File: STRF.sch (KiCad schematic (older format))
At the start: 38 parts, among them J1 USB_B_Micro, J2 SMA, J3 ARM 10pin, U1 XC6206P332MR, U2 USBLC6-2SC6, U3 STM32L432KBU6, U4 nRF24L01P, Y1 16MHz

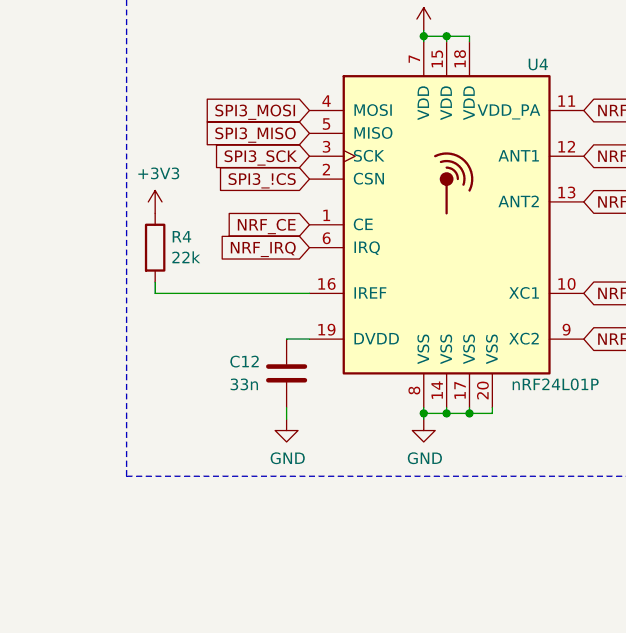
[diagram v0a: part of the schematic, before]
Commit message: Fixed IREF resistor to pull-down.
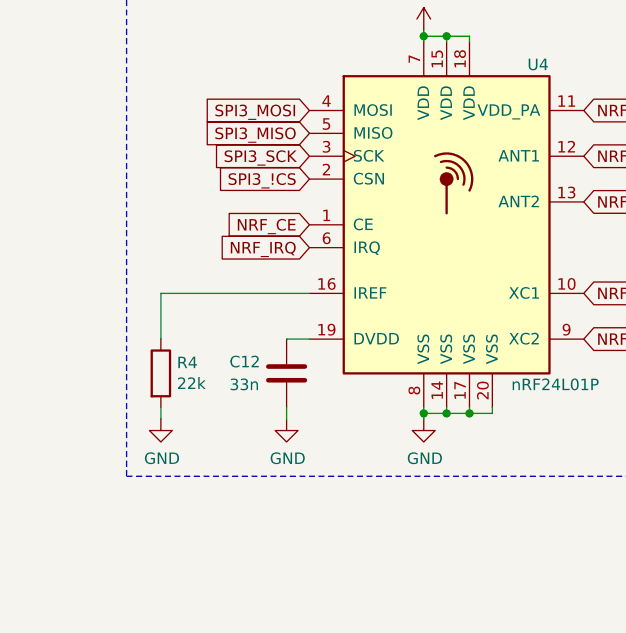
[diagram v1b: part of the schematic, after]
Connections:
- net +3V3: no longer R4.1
- net GND: now also R4.2
- net at U4.16 (IREF): now also R4.1; no longer R4.2
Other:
- moved on the sheet: R4
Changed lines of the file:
@@
 L Device:R R4
 U 1 1 5EC65DFA
-P 1075 5550
-F 0 "R4" H 1145 5596 50  0000 L CNN
-F 1 "22k" H 1145 5505 50  0000 L CNN
-F 2 "Resistor_SMD:R_0402_1005Metric" V 1005 5550 50  0001 C CNN
-F 3 "~" H 1075 5550 50  0001 C CNN
-	1    1075 5550
-	1    0    0    -1
-$EndComp
-Wire Wire Line
-	1750 5750 1075 5750
-Wire Wire Line
-	1075 5750 1075 5700
-$Comp
-L power:+3V3 #PWR022
-U 1 1 5EC6880F
-P 1075 5400
-F 0 "#PWR022" H 1075 5250 50  0001 C CNN
-F 1 "+3V3" H 1090 5573 50  0000 C CNN
-F 2 "" H 1075 5400 50  0001 C CNN
-F 3 "" H 1075 5400 50  0001 C CNN
-	1    1075 5400
+P 1100 6100
+F 0 "R4" H 1170 6146 50  0000 L CNN
+F 1 "22k" H 1170 6055 50  0000 L CNN
+F 2 "Resistor_SMD:R_0402_1005Metric" V 1030 6100 50  0001 C CNN
+F 3 "~" H 1100 6100 50  0001 C CNN
+	1    1100 6100
 	1    0    0    -1
 $EndComp
@@
 	1    0    0    -1
 $EndComp
+Wire Wire Line
+	1100 5950 1100 5750
+Wire Wire Line
+	1100 5750 1750 5750
+$Comp
+L power:GND #PWR?
+U 1 1 5EBE0211
+P 1100 6300
+F 0 "#PWR?" H 1100 6050 50  0001 C CNN
+F 1 "GND" H 1105 6127 50  0000 C CNN
+F 2 "" H 1100 6300 50  0001 C CNN
+F 3 "" H 1100 6300 50  0001 C CNN
+	1    1100 6300
+	1    0    0    -1
+$EndComp
+Wire Wire Line
+	1100 6300 1100 6250
 $EndSCHEMATC

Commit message: Changed USB connector.
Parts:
- J1: footprint Connector_USB:USB_Micro-B_Molex-105017-0001 -> 10118193-0001LF:101181930001LF
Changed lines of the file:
@@
 F 0 "J1" H 4157 1992 50  0000 C CNN
 F 1 "USB_B_Micro" H 4157 1901 50  0000 C CNN
-F 2 "Connector_USB:USB_Micro-B_Molex-105017-0001" H 4250 1475 50  0001 C CNN
+F 2 "10118193-0001LF:101181930001LF" H 4250 1475 50  0001 C CNN
 F 3 "~" H 4250 1475 50  0001 C CNN
 	1    4100 1525
@@
 	1100 5750 1750 5750
 $Comp
-L power:GND #PWR?
+L power:GND #PWR0101
 U 1 1 5EBE0211
 P 1100 6300
-F 0 "#PWR?" H 1100 6050 50  0001 C CNN
+F 0 "#PWR0101" H 1100 6050 50  0001 C CNN
 F 1 "GND" H 1105 6127 50  0000 C CNN
 F 2 "" H 1100 6300 50  0001 C CNN
